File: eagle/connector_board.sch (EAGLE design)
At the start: 22 parts, among them IC1 MEGA8-MI, J1 FH12-6S-0.5SH(55), J2 FH12-6S-0.5SH(55), J3 FH12-6S-0.5SH(55), J4 FH12-6S-0.5SH(55), X4 POGOPIN-CONNWITHVIAS-SMV, X6 POGOPIN-CONNWITHVIAS-SMV

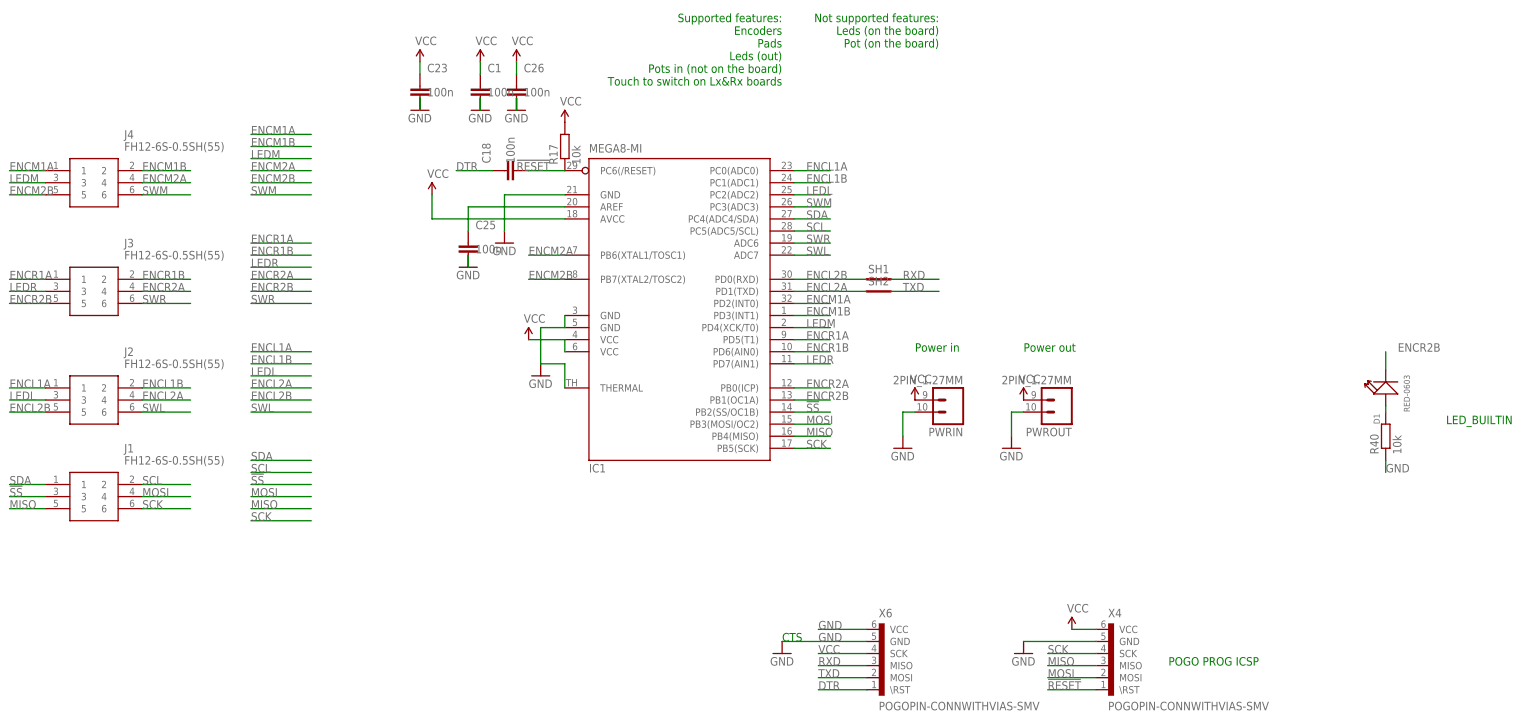
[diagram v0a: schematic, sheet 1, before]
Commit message: Board version 4 WIP;
* Added solder pads to FFC connectors
* Fixed naming of connectors (previously M was on the right and labels
  were wrong
* Flipped builtin led (D1) around to make it safer to use with encoders
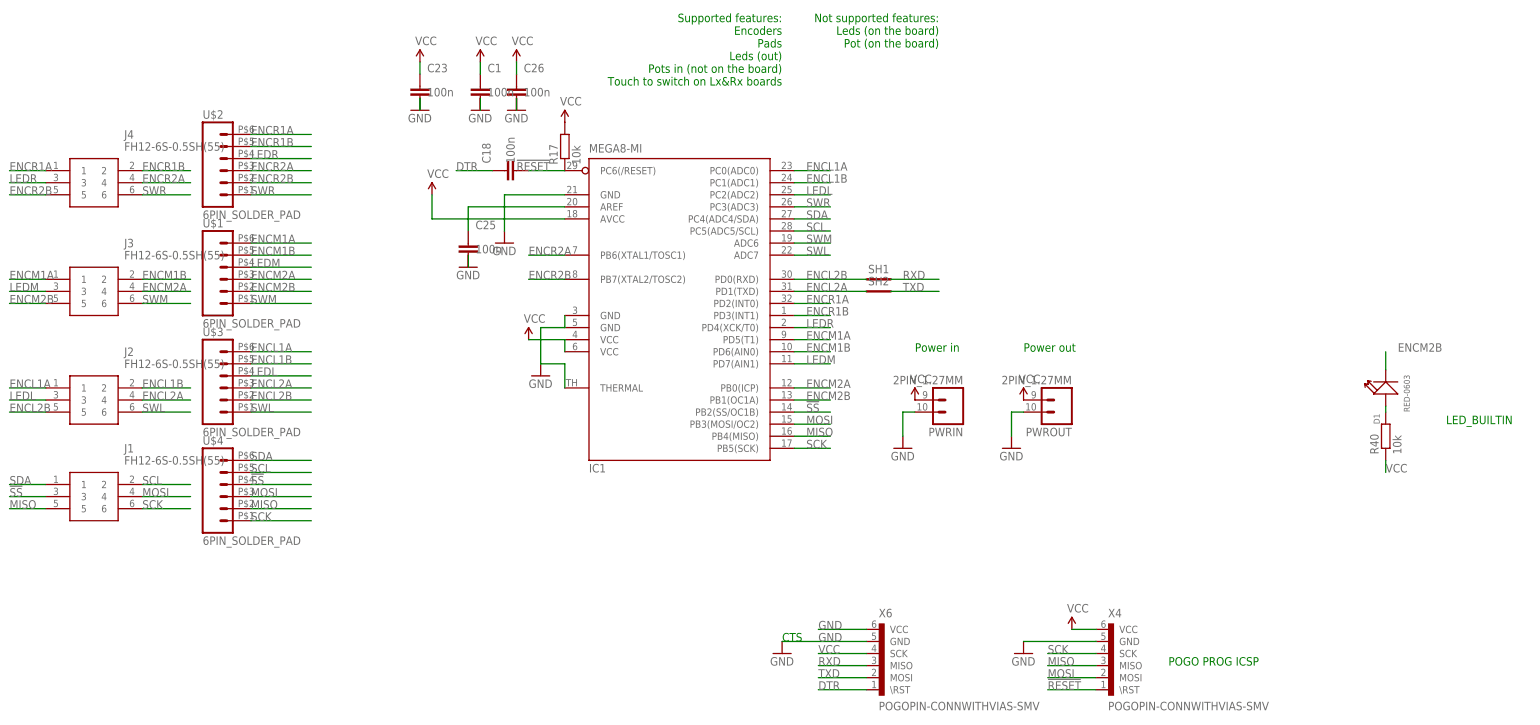
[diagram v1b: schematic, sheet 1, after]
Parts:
- added U$1, U$2, U$3, U$4: 6PIN_SOLDER_PAD, edge:6PIN_SOLDER_PAD
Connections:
- net !SS: now also U$4.4
- net ENCL1A: now also U$3.6
- net ENCL1B: now also U$3.5
- net ENCL2A: now also U$3.3
- net ENCL2B: now also U$3.2
- net ENCM1A: now also IC1.PD5(T1), J3.1, U$1.6; no longer IC1.PD2(INT0), J4.1
- net ENCM1B: now also IC1.PD6(AIN0), J3.2, U$1.5; no longer IC1.PD3(INT1), J4.2
- net ENCM2A: now also IC1.PB0(ICP), J3.4, U$1.3; no longer IC1.PB6(XTAL1/TOSC1), J4.4
- net ENCM2B: now also D1.-, IC1.PB1(OC1A), J3.5, U$1.2; no longer IC1.PB7(XTAL2/TOSC2), J4.5
- net ENCR1A: now also IC1.PD2(INT0), J4.1, U$2.6; no longer IC1.PD5(T1), J3.1
- net ENCR1B: now also IC1.PD3(INT1), J4.2, U$2.5; no longer IC1.PD6(AIN0), J3.2
- net ENCR2A: now also IC1.PB6(XTAL1/TOSC1), J4.4, U$2.3; no longer IC1.PB0(ICP), J3.4
- net ENCR2B: now also IC1.PB7(XTAL2/TOSC2), J4.5, U$2.2; no longer D1.-, IC1.PB1(OC1A), J3.5
- net GND: no longer R40.1
- net LEDL: now also U$3.4
- net LEDM: now also IC1.PD7(AIN1), J3.3, U$1.4; no longer IC1.PD4(XCK/T0), J4.3
- net LEDR: now also IC1.PD4(XCK/T0), J4.3, U$2.4; no longer IC1.PD7(AIN1), J3.3
- net MISO: now also U$4.2
- net MOSI: now also U$4.3
- net SCK: now also U$4.1
- net SCL: now also U$4.5
- net SDA: now also U$4.6
- net SWL: now also U$3.1
- net SWM: now also IC1.ADC6, J3.6, U$1.1; no longer IC1.PC3(ADC3), J4.6
- net SWR: now also IC1.PC3(ADC3), J4.6, U$2.1; no longer IC1.ADC6, J3.6
- net VCC: now also R40.1

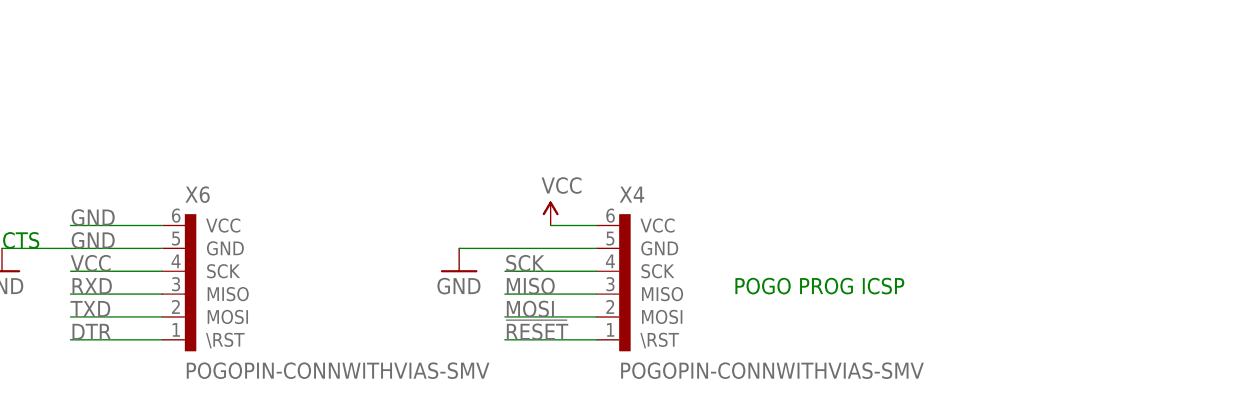
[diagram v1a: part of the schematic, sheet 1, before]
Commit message: Add pogoprog pads on both sides of board
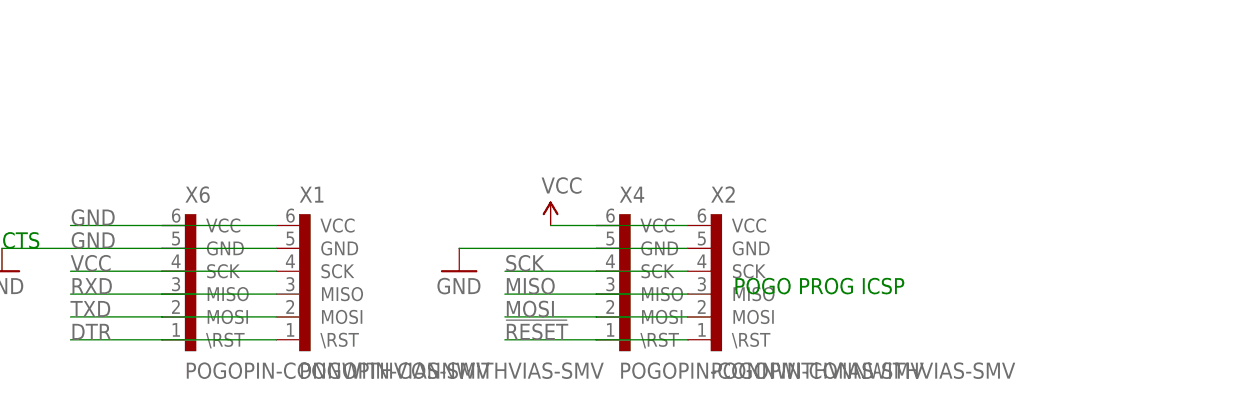
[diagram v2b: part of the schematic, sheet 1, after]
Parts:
- added X1, X2: POGOPIN-CONNWITHVIAS-SMV, Protofusion:POGOPIN-CONNWITHVIAS-SMV
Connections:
- net !RESET: now also X2.\RST
- net DTR: now also X1.\RST
- net GND: now also X1.GND, X1.VCC, X2.GND
- net MISO: now also X2.MISO
- net MOSI: now also X2.MOSI
- net RXD: now also X1.MISO
- net SCK: now also X2.SCK
- net TXD: now also X1.MOSI
- net VCC: now also X1.SCK, X2.VCC
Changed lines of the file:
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@@
 <part name="U$3" library="edge" deviceset="6PIN_SOLDER_PAD" device=""/>
 <part name="U$4" library="edge" deviceset="6PIN_SOLDER_PAD" device=""/>
+<part name="X1" library="Protofusion" deviceset="POGOPIN-CONN" device="WITHVIAS-SMV"/>
+<part name="X2" library="Protofusion" deviceset="POGOPIN-CONN" device="WITHVIAS-SMV"/>
 </parts>
 <sheets>
@@
 <attribute name="NAME" x="-2.54" y="-164.338" size="1.778" layer="95"/>
 </instance>
+<instance part="X1" gate="J" x="152.4" y="-208.28" smashed="yes">
+<attribute name="NAME" x="152.4" y="-200.66" size="1.778" layer="95"/>
+<attribute name="VALUE" x="152.4" y="-218.44" size="1.778" layer="95" rot="MR180"/>
+</instance>
+<instance part="X2" gate="J" x="198.12" y="-208.28" smashed="yes">
+<attribute name="NAME" x="198.12" y="-200.66" size="1.778" layer="95"/>
+<attribute name="VALUE" x="198.12" y="-218.44" size="1.778" layer="95" rot="MR180"/>
+</instance>
 </instances>
 <busses>
@@
 <wire x1="185.42" y1="-205.74" x2="170.18" y2="-205.74" width="0.1524" layer="91"/>
 <pinref part="GND31" gate="1" pin="GND"/>
+<pinref part="X2" gate="J" pin="GND"/>
+<wire x1="185.42" y1="-205.74" x2="195.58" y2="-205.74" width="0.1524" layer="91"/>
 </segment>
 <segment>
@@
 <wire x1="137.16" y1="-203.2" x2="127" y2="-203.2" width="0.1524" layer="91"/>
 <label x="127" y="-203.2" size="1.778" layer="95"/>
+<pinref part="X1" gate="J" pin="VCC"/>
+<wire x1="137.16" y1="-203.2" x2="149.86" y2="-203.2" width="0.1524" layer="91"/>
 </segment>
 <segment>
@@
 <label x="127" y="-205.74" size="1.778" layer="95"/>
 <pinref part="GND3" gate="1" pin="GND"/>
+<pinref part="X1" gate="J" pin="GND"/>
+<wire x1="149.86" y1="-205.74" x2="137.16" y2="-205.74" width="0.1524" layer="91"/>
 </segment>
 </net>
@@
 <wire x1="185.42" y1="-203.2" x2="180.34" y2="-203.2" width="0.1524" layer="91"/>
 <pinref part="SUPPLY8" gate="G$1" pin="VCC"/>
+<pinref part="X2" gate="J" pin="VCC"/>
+<wire x1="195.58" y1="-203.2" x2="185.42" y2="-203.2" width="0.1524" layer="91"/>
 </segment>
 <segment>
@@
 <wire x1="137.16" y1="-208.28" x2="127" y2="-208.28" width="0.1524" layer="91"/>
 <label x="127" y="-208.28" size="1.778" layer="95"/>
+<pinref part="X1" gate="J" pin="SCK"/>
+<wire x1="137.16" y1="-208.28" x2="149.86" y2="-208.28" width="0.1524" layer="91"/>
 </segment>
 <segment>
@@
 <wire x1="185.42" y1="-210.82" x2="175.26" y2="-210.82" width="0.1524" layer="91"/>
 <label x="175.26" y="-210.82" size="1.778" layer="95"/>
+<pinref part="X2" gate="J" pin="MISO"/>
+<wire x1="185.42" y1="-210.82" x2="195.58" y2="-210.82" width="0.1524" layer="91"/>
 </segment>
 <segment>
@@
 <wire x1="185.42" y1="-213.36" x2="175.26" y2="-213.36" width="0.1524" layer="91"/>
 <label x="175.26" y="-213.36" size="1.778" layer="95"/>
+<pinref part="X2" gate="J" pin="MOSI"/>
+<wire x1="195.58" y1="-213.36" x2="185.42" y2="-213.36" width="0.1524" layer="91"/>
 </segment>
 <segment>
@@
 <wire x1="185.42" y1="-208.28" x2="175.26" y2="-208.28" width="0.1524" layer="91"/>
 <label x="175.26" y="-208.28" size="1.778" layer="95"/>
+<pinref part="X2" gate="J" pin="SCK"/>
+<wire x1="195.58" y1="-208.28" x2="185.42" y2="-208.28" width="0.1524" layer="91"/>
 </segment>
 <segment>
@@
 <wire x1="185.42" y1="-215.9" x2="175.26" y2="-215.9" width="0.1524" layer="91"/>
 <label x="175.26" y="-215.9" size="1.778" layer="95"/>
+<pinref part="X2" gate="J" pin="\RST"/>
+<wire x1="185.42" y1="-215.9" x2="195.58" y2="-215.9" width="0.1524" layer="91"/>
 </segment>
 </net>
@@
 <wire x1="137.16" y1="-215.9" x2="127" y2="-215.9" width="0.1524" layer="91"/>
 <label x="127" y="-215.9" size="1.778" layer="95"/>
+<pinref part="X1" gate="J" pin="\RST"/>
+<wire x1="149.86" y1="-215.9" x2="137.16" y2="-215.9" width="0.1524" layer="91"/>
 </segment>
 </net>
@@
 <wire x1="137.16" y1="-210.82" x2="127" y2="-210.82" width="0.1524" layer="91"/>
 <label x="127" y="-210.82" size="1.778" layer="95"/>
+<pinref part="X1" gate="J" pin="MISO"/>
+<wire x1="149.86" y1="-210.82" x2="137.16" y2="-210.82" width="0.1524" layer="91"/>
 </segment>
 </net>
@@
 <wire x1="137.16" y1="-213.36" x2="127" y2="-213.36" width="0.1524" layer="91"/>
 <label x="127" y="-213.36" size="1.778" layer="95"/>
-</segment>
-</net>
+<pinref part="X1" gate="J" pin="MOSI"/>
+<wire x1="137.16" y1="-213.36" x2="149.86" y2="-213.36" width="0.1524" layer="91"/>
+</segment>
+</net>

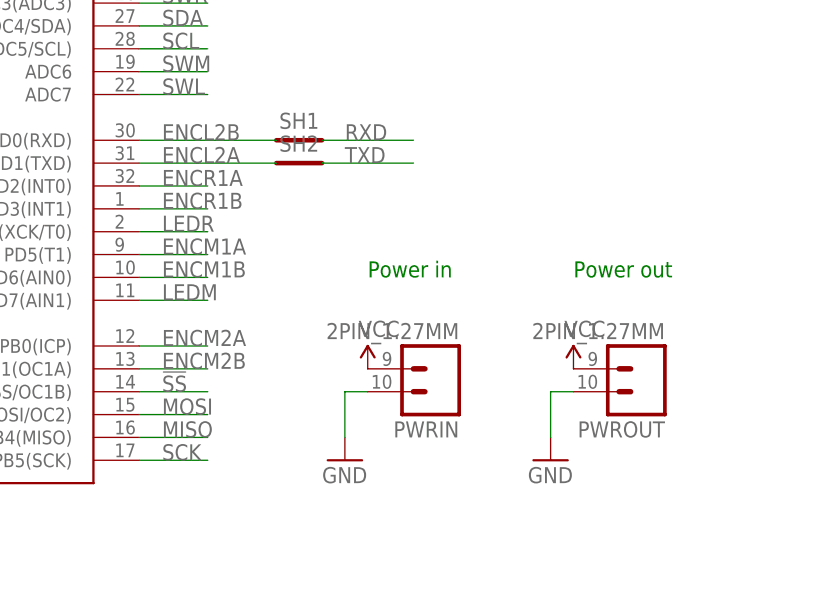
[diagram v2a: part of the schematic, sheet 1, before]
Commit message: Make room for v-score on the edges by rotating connectors 45degs
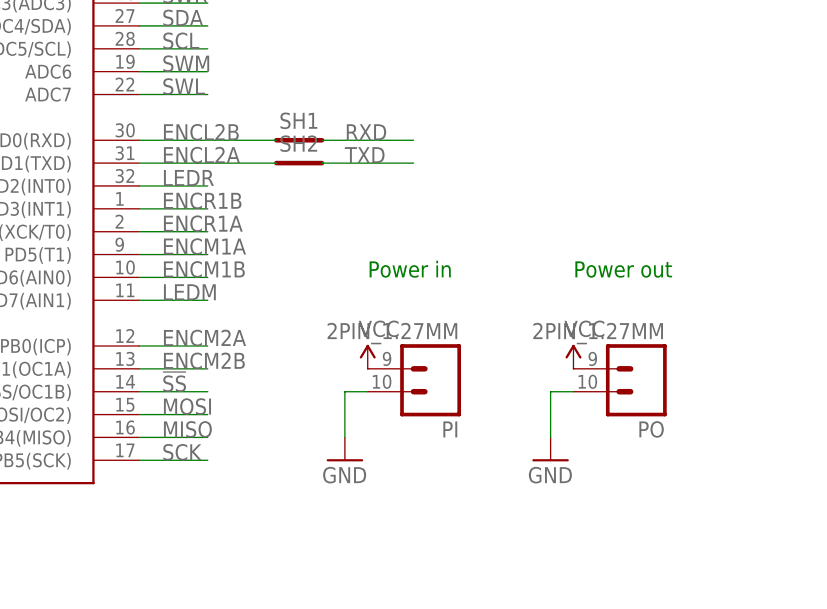
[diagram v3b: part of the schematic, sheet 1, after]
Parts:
- renumbered PWRIN to PI, PWROUT to PO
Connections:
- net ENCR1A: now also IC1.PD4(XCK/T0); no longer IC1.PD2(INT0)
- net LEDR: now also IC1.PD2(INT0); no longer IC1.PD4(XCK/T0)
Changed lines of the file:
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@@
 </classes>
 <parts>
-<part name="PWRIN" library="edge" deviceset="2PIN_1.27MM" device=""/>
+<part name="PI" library="edge" deviceset="2PIN_1.27MM" device=""/>
 <part name="GND6" library="SparkFun-Aesthetics" deviceset="GND" device=""/>
 <part name="C23" library="rcl" library_urn="urn:adsk.eagle:library:334" deviceset="C-EU" device="C0603" package3d_urn="urn:adsk.eagle:package:23616/2" value="100n"/>
@@
 <part name="SH1" library="shorts" deviceset="SHORT" device=""/>
 <part name="SH2" library="shorts" deviceset="SHORT" device=""/>
-<part name="PWROUT" library="edge" deviceset="2PIN_1.27MM" device=""/>
+<part name="PO" library="edge" deviceset="2PIN_1.27MM" device=""/>
 <part name="GND1" library="SparkFun-Aesthetics" deviceset="GND" device=""/>
 <part name="SUPPLY3" library="SparkFun-Aesthetics" deviceset="VCC" device=""/>
@@
 </plain>
 <instances>
-<instance part="PWRIN" gate="G$1" x="154.94" y="-154.94" smashed="yes" rot="R180">
+<instance part="PI" gate="G$1" x="154.94" y="-154.94" smashed="yes" rot="R180">
 <attribute name="VALUE" x="157.48" y="-149.86" size="1.778" layer="96" rot="R180"/>
 <attribute name="NAME" x="157.48" y="-160.782" size="1.778" layer="95" rot="R180"/>
@@
 <attribute name="NAME" x="137.4775" y="-130.81" size="1.778" layer="95"/>
 </instance>
-<instance part="PWROUT" gate="G$1" x="177.8" y="-154.94" smashed="yes" rot="R180">
+<instance part="PO" gate="G$1" x="177.8" y="-154.94" smashed="yes" rot="R180">
 <attribute name="VALUE" x="180.34" y="-149.86" size="1.778" layer="96" rot="R180"/>
 <attribute name="NAME" x="180.34" y="-160.782" size="1.778" layer="95" rot="R180"/>
@@
 <net name="GND" class="0">
 <segment>
-<pinref part="PWRIN" gate="G$1" pin="2"/>
+<pinref part="PI" gate="G$1" pin="2"/>
 <pinref part="GND6" gate="1" pin="GND"/>
 <wire x1="147.32" y1="-157.48" x2="144.78" y2="-157.48" width="0.1524" layer="91"/>
@@
 </segment>
 <segment>
-<pinref part="PWROUT" gate="G$1" pin="2"/>
+<pinref part="PO" gate="G$1" pin="2"/>
 <pinref part="GND1" gate="1" pin="GND"/>
 <wire x1="170.18" y1="-157.48" x2="167.64" y2="-157.48" width="0.1524" layer="91"/>
@@
 </segment>
 <segment>
-<pinref part="PWRIN" gate="G$1" pin="1"/>
+<pinref part="PI" gate="G$1" pin="1"/>
 <pinref part="SUPPLY1" gate="G$1" pin="VCC"/>
 </segment>
@@
 </segment>
 <segment>
-<pinref part="PWROUT" gate="G$1" pin="1"/>
+<pinref part="PO" gate="G$1" pin="1"/>
 <pinref part="SUPPLY3" gate="G$1" pin="VCC"/>
 </segment>
@@
 </segment>
 <segment>
+<wire x1="20.32" y1="-99.06" x2="7.62" y2="-99.06" width="0.1524" layer="91"/>
+<label x="7.62" y="-99.06" size="1.778" layer="95"/>
+<pinref part="U$2" gate="G$1" pin="6"/>
+</segment>
+<segment>
+<pinref part="IC1" gate="G$1" pin="PD4(XCK/T0)"/>
+<wire x1="121.92" y1="-139.7" x2="129.54" y2="-139.7" width="0.1524" layer="91"/>
+<label x="124.46" y="-139.7" size="1.778" layer="95"/>
+</segment>
+</net>
+<net name="ENCR1B" class="0">
+<segment>
+<pinref part="J4" gate="G$1" pin="2"/>
+<wire x1="-15.24" y1="-106.68" x2="-5.08" y2="-106.68" width="0.1524" layer="91"/>
+<label x="-15.24" y="-106.68" size="1.778" layer="95"/>
+</segment>
+<segment>
+<pinref part="IC1" gate="G$1" pin="PD3(INT1)"/>
+<wire x1="121.92" y1="-137.16" x2="129.54" y2="-137.16" width="0.1524" layer="91"/>
+<label x="124.46" y="-137.16" size="1.778" layer="95"/>
+</segment>
+<segment>
+<wire x1="20.32" y1="-101.6" x2="7.62" y2="-101.6" width="0.1524" layer="91"/>
+<label x="7.62" y="-101.6" size="1.778" layer="95"/>
+<pinref part="U$2" gate="G$1" pin="5"/>
+</segment>
+</net>
+<net name="SWR" class="0">
+<segment>
+<pinref part="IC1" gate="G$1" pin="PC3(ADC3)"/>
+<wire x1="121.92" y1="-114.3" x2="129.54" y2="-114.3" width="0.1524" layer="91"/>
+<label x="124.46" y="-114.3" size="1.778" layer="95"/>
+</segment>
+<segment>
+<pinref part="J4" gate="G$1" pin="6"/>
+<wire x1="-15.24" y1="-111.76" x2="-5.08" y2="-111.76" width="0.1524" layer="91"/>
+<label x="-15.24" y="-111.76" size="1.778" layer="95"/>
+</segment>
+<segment>
+<pinref part="U$2" gate="G$1" pin="1"/>
+<wire x1="7.62" y1="-111.76" x2="20.32" y2="-111.76" width="0.1524" layer="91"/>
+<label x="7.62" y="-111.76" size="1.778" layer="95"/>
+</segment>
+</net>
+<net name="LEDR" class="0">
+<segment>
+<pinref part="J4" gate="G$1" pin="3"/>
+<wire x1="-35.56" y1="-109.22" x2="-43.18" y2="-109.22" width="0.1524" layer="91"/>
+<label x="-43.18" y="-109.22" size="1.778" layer="95"/>
+</segment>
+<segment>
+<wire x1="20.32" y1="-104.14" x2="7.62" y2="-104.14" width="0.1524" layer="91"/>
+<label x="7.62" y="-104.14" size="1.778" layer="95"/>
+<pinref part="U$2" gate="G$1" pin="4"/>
+</segment>
+<segment>
 <pinref part="IC1" gate="G$1" pin="PD2(INT0)"/>
 <wire x1="121.92" y1="-134.62" x2="129.54" y2="-134.62" width="0.1524" layer="91"/>
 <label x="124.46" y="-134.62" size="1.778" layer="95"/>
 </segment>
-<segment>
-<wire x1="20.32" y1="-99.06" x2="7.62" y2="-99.06" width="0.1524" layer="91"/>
-<label x="7.62" y="-99.06" size="1.778" layer="95"/>
-<pinref part="U$2" gate="G$1" pin="6"/>
-</segment>
-</net>
-<net name="ENCR1B" class="0">
-<segment>
-<pinref part="J4" gate="G$1" pin="2"/>
-<wire x1="-15.24" y1="-106.68" x2="-5.08" y2="-106.68" width="0.1524" layer="91"/>
-<label x="-15.24" y="-106.68" size="1.778" layer="95"/>
-</segment>
-<segment>
-<pinref part="IC1" gate="G$1" pin="PD3(INT1)"/>
-<wire x1="121.92" y1="-137.16" x2="129.54" y2="-137.16" width="0.1524" layer="91"/>
-<label x="124.46" y="-137.16" size="1.778" layer="95"/>
-</segment>
-<segment>
-<wire x1="20.32" y1="-101.6" x2="7.62" y2="-101.6" width="0.1524" layer="91"/>
-<label x="7.62" y="-101.6" size="1.778" layer="95"/>
-<pinref part="U$2" gate="G$1" pin="5"/>
-</segment>
-</net>
-<net name="SWR" class="0">
-<segment>
-<pinref part="IC1" gate="G$1" pin="PC3(ADC3)"/>
-<wire x1="121.92" y1="-114.3" x2="129.54" y2="-114.3" width="0.1524" layer="91"/>
-<label x="124.46" y="-114.3" size="1.778" layer="95"/>
-</segment>
-<segment>
-<pinref part="J4" gate="G$1" pin="6"/>
-<wire x1="-15.24" y1="-111.76" x2="-5.08" y2="-111.76" width="0.1524" layer="91"/>
-<label x="-15.24" y="-111.76" size="1.778" layer="95"/>
-</segment>
-<segment>
-<pinref part="U$2" gate="G$1" pin="1"/>
-<wire x1="7.62" y1="-111.76" x2="20.32" y2="-111.76" width="0.1524" layer="91"/>
-<label x="7.62" y="-111.76" size="1.778" layer="95"/>
-</segment>
-</net>
-<net name="LEDR" class="0">
-<segment>
-<pinref part="IC1" gate="G$1" pin="PD4(XCK/T0)"/>
-<wire x1="121.92" y1="-139.7" x2="129.54" y2="-139.7" width="0.1524" layer="91"/>
-<label x="124.46" y="-139.7" size="1.778" layer="95"/>
-</segment>
-<segment>
-<pinref part="J4" gate="G$1" pin="3"/>
-<wire x1="-35.56" y1="-109.22" x2="-43.18" y2="-109.22" width="0.1524" layer="91"/>
-<label x="-43.18" y="-109.22" size="1.778" layer="95"/>
-</segment>
-<segment>
-<wire x1="20.32" y1="-104.14" x2="7.62" y2="-104.14" width="0.1524" layer="91"/>
-<label x="7.62" y="-104.14" size="1.778" layer="95"/>
-<pinref part="U$2" gate="G$1" pin="4"/>
-</segment>
-</net>
+</net>
